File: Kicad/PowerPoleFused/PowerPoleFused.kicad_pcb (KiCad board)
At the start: 2 copper layers, 96.5 x 43.2 mm, 12 parts, among them J1 Anderson powerpole, J2 Anderson powerpole, J3 Anderson powerpole, J4 Anderson powerpole, J5 Anderson powerpole, J6 Anderson powerpole

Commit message: Laid out board 1st attempt
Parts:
- added D1: LED, LED_THT:LED_D5.0mm, F.Cu at (54.4, 50.8)
- added D2: LED, LED_THT:LED_D5.0mm, F.Cu at (69.6, 50.8)
- added D3: LED, LED_THT:LED_D5.0mm, F.Cu at (85.1, 50.8)
- added D4: LED, LED_THT:LED_D5.0mm, F.Cu at (99.3, 50.8)
- added D5: LED, LED_THT:LED_D5.0mm, F.Cu at (115.3, 50.8)
- added D6: LED, LED_THT:LED_D5.0mm, F.Cu at (130.0, 50.3)
- added F1: SamacSys_Parts_3557-20, Fuses:355720, F.Cu at (54.2, 74.8)
- added F2: SamacSys_Parts_3557-20, Fuses:355720, F.Cu at (69.4, 74.8)
- added F3: SamacSys_Parts_3557-20, Fuses:355720, F.Cu at (84.7, 74.8)
- added F4: SamacSys_Parts_3557-20, Fuses:355720, F.Cu at (100.1, 74.8)
- added F5: SamacSys_Parts_3557-20, Fuses:355720, F.Cu at (115.3, 74.9)
- added F6: SamacSys_Parts_3557-20, Fuses:355720, F.Cu at (130.6, 74.6)
- added R1: 2K2, Resistor_THT:R_Axial_DIN0207_L6.3mm_D2.5mm_P7.62mm_Horizontal, F.Cu at (63.5, 47.8)
- added R2: 2K2, Resistor_THT:R_Axial_DIN0207_L6.3mm_D2.5mm_P7.62mm_Horizontal, F.Cu at (78.2, 55.1)
- added R3: 2K2, Resistor_THT:R_Axial_DIN0207_L6.3mm_D2.5mm_P7.62mm_Horizontal, F.Cu at (93.5, 54.9)
- added R4: 2K2, Resistor_THT:R_Axial_DIN0207_L6.3mm_D2.5mm_P7.62mm_Horizontal, F.Cu at (108.2, 54.4)
- added R5: 2K2, Resistor_THT:R_Axial_DIN0207_L6.3mm_D2.5mm_P7.62mm_Horizontal, F.Cu at (124.5, 54.4)
- added R6: 2K2, Resistor_THT:R_Axial_DIN0207_L6.3mm_D2.5mm_P7.62mm_Horizontal, F.Cu at (136.7, 54.4)
- moved REF** 62.9 mm to (56.1, 105.7)
- moved REF** 62.9 mm to (94.2, 105.7)
- moved J1 62.9 mm to (54.4, 87.6)
- moved J2 62.9 mm to (69.6, 87.6)
- moved J3 62.9 mm to (84.8, 87.6)
- moved J4 62.9 mm to (100.1, 87.6)
- moved J5 62.9 mm to (115.3, 87.6)
- moved J6 62.9 mm to (130.6, 87.6)
- moved REF** 62.9 mm to (132.3, 105.7)
- moved REF** 31.5 mm to (93.5, 39.6)
- moved REF** 30.8 mm to (131.1, 39.1)
- moved REF** 30.7 mm to (54.4, 39.6)
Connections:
- net Net-(J1--ve) renamed 0
- J2 pad 1: Net-(J1-+ve) -> Net-(J2-+ve)
- J3 pad 1: Net-(J1-+ve) -> Net-(J3-+ve)
- J4 pad 1: Net-(J1-+ve) -> Net-(J4-+ve)
- J5 pad 1: Net-(J1-+ve) -> Net-(J5-+ve)
- J6 pad 1: Net-(J1-+ve) -> Net-(J6-+ve)
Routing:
- net 0: track 0.00 -> 141.3 mm
- net Net-(J4-+ve): track 0.00 -> 90.8 mm
- net Net-(J6-+ve): track 0.00 -> 90.6 mm
- net Net-(J1-+ve): track 0.00 -> 87.3 mm
- net Net-(J3-+ve): track 0.00 -> 81.3 mm
- net Net-(J5-+ve): track 0.00 -> 81.2 mm
- net Net-(J2-+ve): track 0.00 -> 80.7 mm
- net Net-(D5-A): track 0.00 -> 8.29 mm
- net Net-(D4-A): track 0.00 -> 8.04 mm
- net Net-(D1-A): track 0.00 -> 7.87 mm
- net Net-(D2-A): track 0.00 -> 7.46 mm
- net Net-(D3-A): track 0.00 -> 7.32 mm
- net Net-(D6-A): track 0.00 -> 5.54 mm
- added copper zone on B.Cu, net +12V
- added copper zone on F.Cu, net +12V
- removed copper zone on B.Cu, net Net-(J1-+ve)
- removed copper zone on F.Cu, net Net-(J1-+ve)
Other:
- board size 96.5 x 43.2 mm -> 96.8 x 83.3 mm

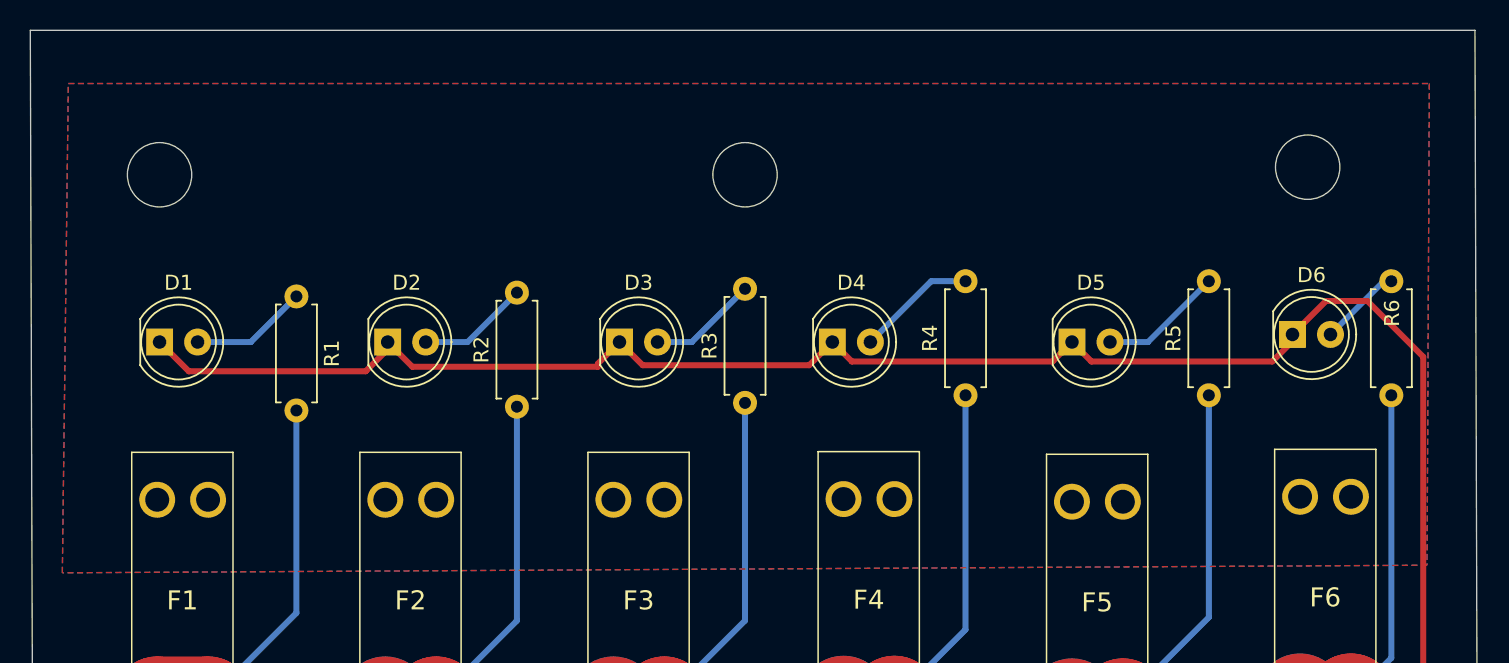
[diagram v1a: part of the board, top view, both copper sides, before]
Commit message: Better routing of +ve layer
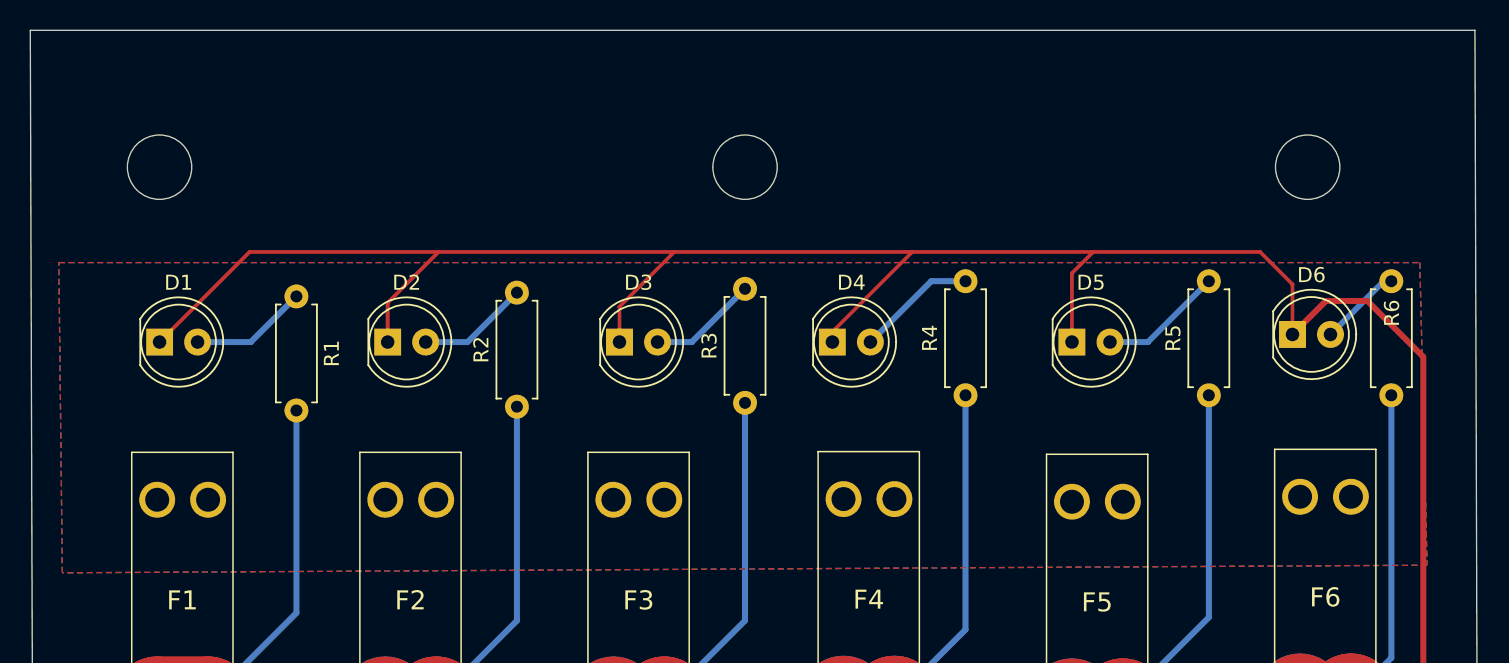
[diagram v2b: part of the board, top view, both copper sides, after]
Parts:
- moved REF** 0.51 mm to (54.4, 39.1)
- moved REF** 0.51 mm to (93.5, 39.1)
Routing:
- net 0: track 141.3 -> 171.5 mm
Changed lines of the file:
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@@
 		(tags "Undefined or Miscellaneous")
 		(property "Reference" "F5"
-			(at 6.735 1.683 360)
+			(at 6.735 1.683 0)
 			(layer "F.SilkS")
 			(effects
@@
 	(footprint "MountingHole:MountingHole_4.3mm_M4_DIN965"
 		(layer "F.Cu")
-		(at 54.356 39.624)
+		(at 54.356 39.116)
 		(descr "Mounting Hole 4.3mm, no annular, M4, DIN965")
 		(tags "mounting hole 4.3mm no annular m4 din965")
@@
 	(footprint "MountingHole:MountingHole_4.3mm_M4_DIN965"
 		(layer "F.Cu")
-		(at 93.472 39.624)
+		(at 93.472 39.116)
 		(descr "Mounting Hole 4.3mm, no annular, M4, DIN965")
 		(tags "mounting hole 4.3mm no annular m4 din965")
@@
 		(tags "Undefined or Miscellaneous")
 		(property "Reference" "F6"
-			(at 6.735 1.683 360)
+			(at 6.735 1.683 0)
 			(layer "F.SilkS")
 			(effects
@@
 	)
 	(segment
-		(start 115.316 50.8)
-		(end 116.616 52.1)
-		(width 0.4)
+		(start 130.048 46.9392)
+		(end 127.889 44.7802)
+		(width 0.25)
 		(layer "F.Cu")
 		(net 13)
 	)
 	(segment
-		(start 99.309 50.8)
-		(end 100.609 52.1)
+		(start 130.556 95.254)
+		(end 138.7856 87.0244)
 		(width 0.4)
 		(layer "F.Cu")
@@
 	)
 	(segment
-		(start 71.247 52.451)
-		(end 83.6422 52.451)
+		(start 135.0518 48.0568)
+		(end 132.2832 48.0568)
 		(width 0.4)
 		(layer "F.Cu")
@@
 	)
 	(segment
-		(start 130.556 95.254)
-		(end 138.7856 87.0244)
-		(width 0.4)
+		(start 88.7476 44.7802)
+		(end 72.9996 44.7802)
+		(width 0.25)
 		(layer "F.Cu")
 		(net 13)
 	)
 	(segment
-		(start 68.1228 52.7558)
-		(end 69.596 51.2826)
-		(width 0.4)
+		(start 99.309 50.1192)
+		(end 104.648 44.7802)
+		(width 0.25)
 		(layer "F.Cu")
 		(net 13)
 	)
 	(segment
-		(start 135.0518 48.0568)
-		(end 132.2832 48.0568)
-		(width 0.4)
+		(start 60.3758 44.7802)
+		(end 54.356 50.8)
+		(width 0.25)
 		(layer "F.Cu")
 		(net 13)
 	)
 	(segment
-		(start 83.6422 52.451)
-		(end 83.6422 52.2428)
-		(width 0.4)
+		(start 127.889 44.7802)
+		(end 116.7384 44.7802)
+		(width 0.25)
 		(layer "F.Cu")
 		(net 13)
 	)
 	(segment
-		(start 116.616 52.1)
-		(end 128.6972 52.1)
-		(width 0.4)
+		(start 72.9996 44.7802)
+		(end 60.3758 44.7802)
+		(width 0.25)
 		(layer "F.Cu")
 		(net 13)
 	)
 	(segment
-		(start 54.356 50.8)
-		(end 56.3118 52.7558)
-		(width 0.4)
+		(start 104.648 44.7802)
+		(end 88.7476 44.7802)
+		(width 0.25)
 		(layer "F.Cu")
 		(net 13)
 	)
 	(segment
-		(start 85.085 50.8)
-		(end 86.6344 52.3494)
-		(width 0.4)
+		(start 130.048 50.292)
+		(end 130.048 46.9392)
+		(width 0.25)
 		(layer "F.Cu")
 		(net 13)
@@
 	)
 	(segment
-		(start 83.6422 52.2428)
-		(end 85.085 50.8)
-		(width 0.4)
+		(start 69.596 50.8)
+		(end 69.596 48.1838)
+		(width 0.25)
 		(layer "F.Cu")
 		(net 13)
@@
 	)
 	(segment
-		(start 114.016 52.1)
-		(end 115.316 50.8)
-		(width 0.4)
+		(start 85.085 50.8)
+		(end 85.085 48.4428)
+		(width 0.25)
 		(layer "F.Cu")
 		(net 13)
 	)
 	(segment
-		(start 56.3118 52.7558)
-		(end 68.1228 52.7558)
-		(width 0.4)
+		(start 115.316 50.8)
+		(end 115.316 46.2026)
+		(width 0.25)
 		(layer "F.Cu")
 		(net 13)
 	)
 	(segment
-		(start 132.2832 48.0568)
-		(end 130.048 50.292)
-		(width 0.4)
+		(start 99.309 50.8)
+		(end 99.309 50.1192)
+		(width 0.25)
 		(layer "F.Cu")
 		(net 13)
 	)
 	(segment
-		(start 100.609 52.1)
-		(end 114.016 52.1)
-		(width 0.4)
+		(start 69.596 48.1838)
+		(end 72.9996 44.7802)
+		(width 0.25)
 		(layer "F.Cu")
 		(net 13)
 	)
 	(segment
-		(start 69.596 50.8)
-		(end 71.247 52.451)
-		(width 0.4)
+		(start 116.7384 44.7802)
+		(end 104.648 44.7802)
+		(width 0.25)
 		(layer "F.Cu")
 		(net 13)
 	)
 	(segment
-		(start 138.7856 51.7906)
-		(end 135.0518 48.0568)
+		(start 132.2832 48.0568)
+		(end 130.048 50.292)
 		(width 0.4)
 		(layer "F.Cu")
@@
 	)
 	(segment
-		(start 86.6344 52.3494)
-		(end 97.7596 52.3494)
-		(width 0.4)
+		(start 115.316 46.2026)
+		(end 116.7384 44.7802)
+		(width 0.25)
 		(layer "F.Cu")
 		(net 13)
 	)
 	(segment
-		(start 138.7856 87.0244)
-		(end 138.7856 51.7906)
+		(start 138.7856 51.7906)
+		(end 135.0518 48.0568)
 		(width 0.4)
 		(layer "F.Cu")
@@
 	)
 	(segment
-		(start 128.6972 52.1)
-		(end 130.048 50.7492)
+		(start 138.7856 87.0244)
+		(end 138.7856 51.7906)
 		(width 0.4)
 		(layer "F.Cu")
@@
 	)
 	(segment
-		(start 130.556 95.504)
-		(end 130.556 95.254)
-		(width 0.4)
+		(start 85.085 48.4428)
+		(end 88.7476 44.7802)
+		(width 0.25)
 		(layer "F.Cu")
 		(net 13)
 	)
 	(segment
-		(start 97.7596 52.3494)
-		(end 99.309 50.8)
+		(start 130.556 95.504)
+		(end 130.556 95.254)
 		(width 0.4)
 		(layer "F.Cu")
@@
 		(polygon
 			(pts
-				(xy 48.26 33.528) (xy 139.192 33.528) (xy 139.0396 65.7098) (xy 47.8601 66.2178)
+				(xy 47.625 45.4914) (xy 138.557 45.4914) (xy 139.0396 65.7098) (xy 47.8601 66.2178)
 			)
 		)

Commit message: Alighment of items
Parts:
- added REF**: OSHW-Logo2_9.8x8mm_SilkScreen, Symbol:OSHW-Logo2_9.8x8mm_SilkScreen, F.Cu at (72.9, 37.8)
- moved R1 1.02 mm to (63.5, 46.7)
- moved R2 0.76 mm to (78.2, 54.4)
- moved D6 0.51 mm to (130.0, 50.8)
- moved R3 0.51 mm to (93.5, 54.4)
- moved F5 0.33 mm to (115.3, 74.6)
- moved F1 0.20 mm to (54.2, 74.6)
- moved F2 0.20 mm to (69.4, 74.6)
- moved F3 0.20 mm to (84.7, 74.6)
- moved F4 0.15 mm to (100.1, 74.6)
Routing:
- net Net-(J1-+ve): track 87.3 -> 88.3 mm
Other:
- board text added: "RADARC 6 way fused powerpole https://bit.ly/4hMhlbq"
